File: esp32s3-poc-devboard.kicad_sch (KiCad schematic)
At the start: 112 parts, among them J1 24VDC, J2 Conn_01x01_Pin, J3 USB_C_Receptacle_USB2.0_14P, J4 USB_C_Receptacle_USB2.0_14P, J5 Screw_Terminal_01x06, J6 Conn_Coaxial, J7 Conn_01x16_Pin, J8 Screw_Terminal_01x04, Q3 MMDT5551, SW1 SW_Push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

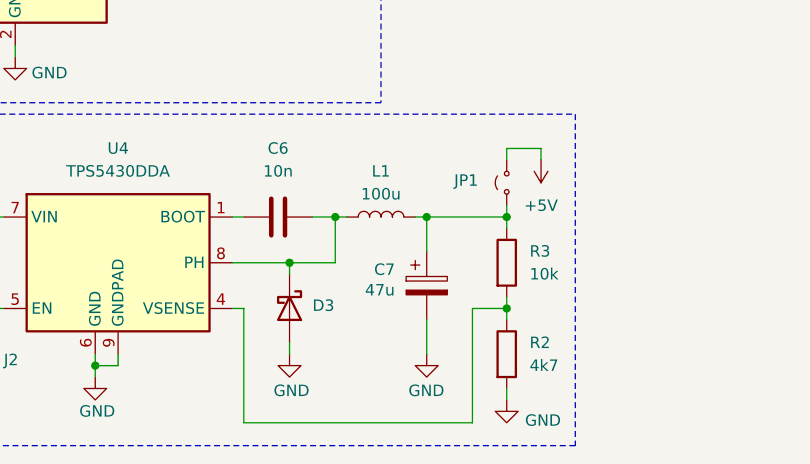
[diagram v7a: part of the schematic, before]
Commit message: schem: replace TPS5430 Cout with basic part
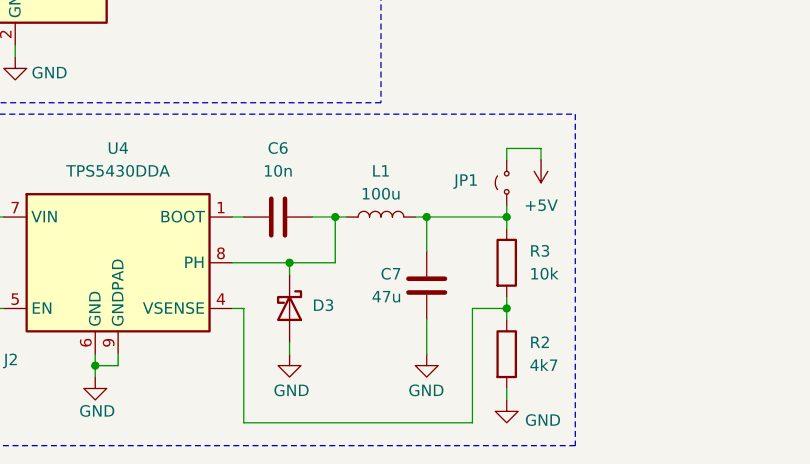
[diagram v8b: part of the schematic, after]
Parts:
- removed C7: 47u, Capacitor_SMD:C_1210_3225Metric, symbol Device:C_Polarized
- added C7: 47u, Capacitor_SMD:C_1206_3216Metric, symbol Device:C
- Q3, R25, R29, R30, R31: Basic P -> E
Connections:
- net GND: now also C7.2
- net at JP1.1 (A), L1.2, R3.1: now also C7.1
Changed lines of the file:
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@@
 			)
 		)
-		(property "Basic" "P"
+		(property "Basic" "E"
 			(at 162.56 99.06 90)
 			(effects
@@
 			)
 		)
-		(property "Basic" "P"
+		(property "Basic" "E"
 			(at 34.29 107.95 0)
 			(effects
@@
 	)
 	(symbol
-		(lib_id "Device:C_Polarized")
-		(at 152.4 176.53 0)
-		(unit 1)
-		(exclude_from_sim no)
-		(in_bom yes)
-		(on_board yes)
-		(dnp no)
-		(property "Reference" "C7"
-			(at 146.558 174.752 0)
-			(effects
-				(font
-					(size 1.27 1.27)
-				)
-				(justify left)
-			)
-		)
-		(property "Value" "47u"
-			(at 145.542 177.038 0)
-			(effects
-				(font
-					(size 1.27 1.27)
-				)
-				(justify left)
-			)
-		)
-		(property "Footprint" "Capacitor_SMD:C_1210_3225Metric"
-			(at 153.3652 180.34 0)
-			(effects
-				(font
-					(size 1.27 1.27)
-				)
-				(hide yes)
-			)
-		)
-		(property "Datasheet" "~"
-			(at 152.4 176.53 0)
-			(effects
-				(font
-					(size 1.27 1.27)
-				)
-				(hide yes)
-			)
-		)
-		(property "Description" "Polarized capacitor"
-			(at 152.4 176.53 0)
-			(effects
-				(font
-					(size 1.27 1.27)
-				)
-				(hide yes)
-			)
-		)
-		(property "Manufacturer" "Panasonic"
-			(at 152.4 176.53 0)
-			(effects
-				(font
-					(size 1.27 1.27)
-				)
-				(hide yes)
-			)
-		)
-		(property "Manufacturer Part Number" "10TPE47MAZB"
-			(at 152.4 176.53 0)
-			(effects
-				(font
-					(size 1.27 1.27)
-				)
-				(hide yes)
-			)
-		)
-		(property "Basic" "X"
-			(at 152.4 176.53 0)
-			(effects
-				(font
-					(size 1.27 1.27)
-				)
-				(hide yes)
-			)
-		)
-		(property "JLCPCB Part #" "C147768"
-			(at 152.4 176.53 0)
-			(effects
-				(font
-					(size 1.27 1.27)
-				)
-				(hide yes)
-			)
-		)
-		(pin "1"
-		)
-		(pin "2"
-		)
-		(instances
-			(project ""
-				(path "/a6beb550-83d0-4746-bc61-cde76b7466a3"
-					(reference "C7")
-					(unit 1)
-				)
-			)
-		)
-	)
-	(symbol
 		(lib_id "Device:LED")
 		(at 59.69 163.83 0)
@@
 			)
 		)
-		(property "Basic" "P"
+		(property "Basic" "E"
 			(at 162.56 101.6 90)
 			(effects
@@
 			)
 		)
-		(property "Basic" "P"
+		(property "Basic" "E"
 			(at 162.56 104.14 90)
 			(effects
@@
 			)
 		)
-		(property "Basic" "P"
+		(property "Basic" "E"
 			(at 48.26 97.79 0)
 			(effects
@@
 			)
 		)
-		(property "Basic" "P"
+		(property "Basic" "E"
 			(at 162.56 106.68 90)
 			(effects
@@
 					(unit 1)
 				)
+			)
+		)
+	)
+	(symbol
+		(lib_id "Device:C")
+		(at 152.4 176.53 0)
+		(mirror y)
+		(unit 1)
+		(exclude_from_sim no)
+		(in_bom yes)
+		(on_board yes)
+		(dnp no)
+		(property "Reference" "C7"
+			(at 149.606 175.26 0)
+			(effects
+				(font
+					(size 1.27 1.27)
+				)
+				(justify left)
+			)
+		)
+		(property "Value" "47u"
+			(at 149.606 177.8 0)
+			(effects
+				(font
+					(size 1.27 1.27)
+				)
+				(justify left)
+			)
+		)
+		(property "Footprint" "Capacitor_SMD:C_1206_3216Metric"
+			(at 151.4348 180.34 0)
+			(effects
+				(font
+					(size 1.27 1.27)
+				)
+				(hide yes)
+			)
+		)
+		(property "Datasheet" "~"
+			(at 152.4 176.53 0)
+			(effects
+				(font
+					(size 1.27 1.27)
+				)
+				(hide yes)
+			)
+		)
+		(property "Description" "Unpolarized capacitor"
+			(at 152.4 176.53 0)
+			(effects
+				(font
+					(size 1.27 1.27)
+				)
+				(hide yes)
+			)
+		)
+		(property "Basic" "Y"
+			(at 152.4 176.53 0)
+			(effects
+				(font
+					(size 1.27 1.27)
+				)
+				(hide yes)
+			)
+		)
+		(property "JLCPCB Part #" "C96123"
+			(at 152.4 176.53 0)
+			(effects
+				(font
+					(size 1.27 1.27)
+				)
+				(hide yes)
+			)
+		)
+		(property "Manufacturer" "Samsung Electro-Mechanics "
+			(at 152.4 176.53 0)
+			(effects
+				(font
+					(size 1.27 1.27)
+				)
+				(hide yes)
+			)
+		)
+		(property "Manufacturer Part Number" "CL31A476MPHNNNE"
+			(at 152.4 176.53 0)
+			(effects
+				(font
+					(size 1.27 1.27)
+				)
+				(hide yes)
+			)
+		)
+		(pin "2"
+		)
+		(pin "1"
+		)
+		(instances
+			(project "esp32s3-poc-devboard"
+				(path "/a6beb550-83d0-4746-bc61-cde76b7466a3"
+					(reference "C7")
+					(unit 1)
+				)
